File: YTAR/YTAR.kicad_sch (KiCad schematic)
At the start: 241 parts, among them J1 STDC14, J2 CAMERA, J3 Micro_Sd, J4 FH12-40S-0.5SH(55), J5 USB_C_USB4085-GF-A, J6 IO, SW1 RESET, SW2 PICTURE, SW3 MODE, U1 STM32H750XBHx, U2 MCP2562-E-MF, U3 DS90C124, U5 TPS56339, U6 TPS56339, Y1 25MHz

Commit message: Filled all
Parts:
- C1, C2, C26, C54, C58, C71: MPN LMK105ABJ225KVHF -> LMK105ABJ225KVHF; Mouser TEMPLATE_MOUSER -> 963-LMK105ABJ225KVHF
- C10, C11, C12, C13, C14, C15, C16, C17, C18, C19, C20, C21, C22, C23, C27, C28, C29, C3, C30, C31, C32, C33, C34, C35, C36, C37, C38, C39, C4, C40, C41, C42, C43, C44, C45, C46, C47, C48, C49, C5, C50, C51, C52, C53, C59, C6, C64, C67, C68, C7, C8, C9: Mouser TEMPLATE_MOUSER -> 963-MLASE105SB7104KF
- C24, C25: Mouser TEMPLATE_MOUSER -> 187-CL05A475MR5NQNC
- C55: MPN 04025C472KAT2A -> 04025C472KAT2A; Mouser TEMPLATE_MOUSER -> 581-04025C472KAT2A
- C56, C57: symbol MEMS_CAPACITORS:C_8p2_0402_50V_C0G_04025A8R2CAT2A_ -> MEMS_CAPACITORS:C_8p2_0402_50V_C0G_04025A8R2CAT2A; MPN TEMPLATE_MPN -> 04025A8R2CAT2A; Mouser TEMPLATE_MOUSER -> 581-04025A8R2C
- C60, C61, C69, C70: Mouser TEMPLATE_MOUSER -> 81-GRM21BC81C226ME4L
- C62, C63, C65, C66: Mouser TEMPLATE_MOUSER -> 581-08053D106KAT4A
- D4: Mouser (none) -> 833-BZT52B3V6-TP
- D6: MPN MMSZ4705-HE3_A-08 -> MMSZ4705-HE3_A-08; Mouser (none) -> 78-MMSZ4705-HE3_A-08
- F1: Mouser (none) -> 576-0805L035
- J2, J6: MPN DF52-8S-0.8H(21) -> DF52-8S-0.8H(21); Mouser (none) -> 798-DF52-8S-0.8H21
- J3: MPN DM3AT-SF-PEJM5 -> DM3AT-SF-PEJM5; Mouser (none) -> 798-DM3AT-SF-PEJM5
- J4: MPN FH12-40S-0.5SH(55) -> FH12-40S-0.5SH(55); Mouser (none) -> 798-FH12-40S-0.5SH55
- J5: MPN USB4085-GF-A -> USB4085-GF-A; Mouser (none) -> 640-USB4085-GF-A
- L1, L2: Mouser (none) -> 652-SRN6028C-6R0M
- SW1, SW2, SW3: MPN B3U-1000PM -> B3U-1000PM; Mouser (none) -> 653-B3U-1000PM
- U1: MPN STM32H750XBH6 -> STM32H750XBH6; Mouser (none) -> 511-STM32H750XBH6
- U2: symbol Interface_CAN_LIN:MCP2562-E-MF -> MEMS_IC:MCP2562-H-MF; MPN (none) -> MCP2562FDT-H/MF; Mouser (none) -> 579-MCP2562FDT-H/MF
- U3: MPN DS90C124IVS/NOPB -> DS90C124IVS/NOPB; Mouser (none) -> 926-DS90C124IVS/NOPB
- U4: Mouser (none) -> 870-IS42S32400F-6BL
- Y1: MPN 520-250-8-36CKM-TR3 -> ECS-250-8-36CKM-TR3; Mouser ECS-250-8-36CKM-TR3 -> 520-250-8-36CKM-TR3

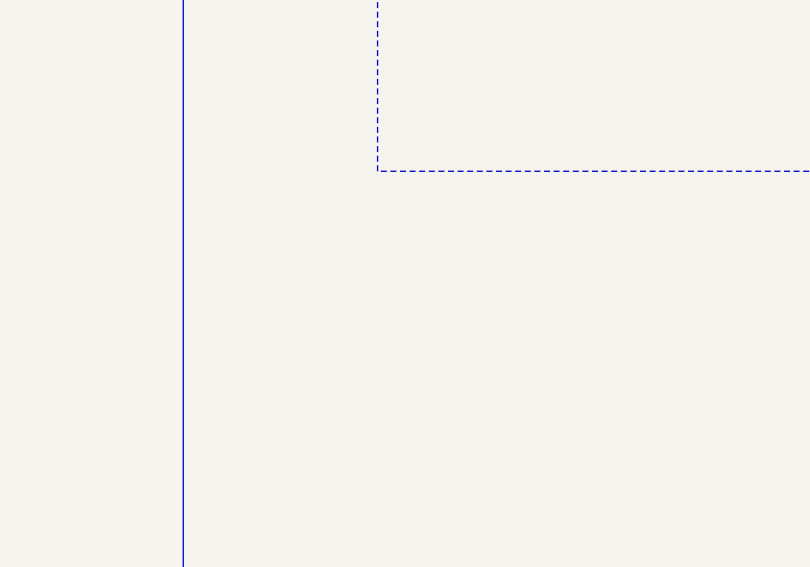
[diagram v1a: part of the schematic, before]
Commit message: Error log added
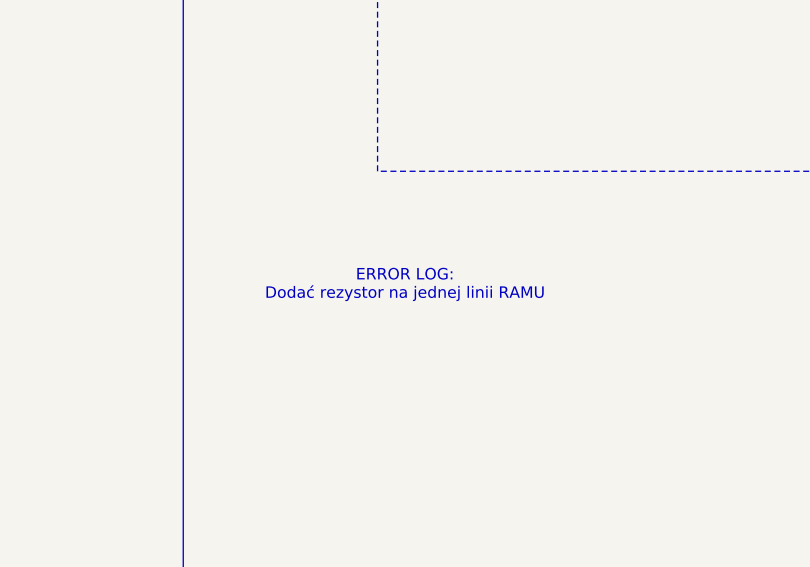
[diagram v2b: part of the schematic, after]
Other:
- note added: "ERROR LOG: Dodać rezystor na jednej linii RAMU"
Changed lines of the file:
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@@
+		)
+	)
+	(text "ERROR LOG:\nDodać rezystor na jednej linii RAMU"
+		(exclude_from_sim no)
+		(at 495.808 365.76 0)
+		(effects
+			(font
+				(size 1.27 1.27)
+			)
 		)
 	)

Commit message: idk
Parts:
- U3: MPN DS90C124IVS/NOPB -> DS90C124IVS/NOPB
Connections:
- net +3.3V: now also U3.7 (VDDOR3); no longer U3.8 (VSSOR3)
- net GND: now also U3.8 (VSSOR3); no longer U3.7 (VDDOR3)
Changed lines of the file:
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@@
 			)
 		)
-		(property "Description" "Serializers & Deserializers - Serdes 5-35MHz 24B FPD Link II Deserializer"
+		(property "Description" "DC-Balanced 24-Bit FPD-Link II Deserializer, TQFP-48"
 			(at 414.02 345.44 0)
 			(effects
@@
 			)
 		)
-		(property "MPN" "DS90C124IVS/NOPB"
+		(property "MPN" " DS90C124IVS/NOPB"
 			(at 387.35 323.8814 0)
 			(effects
